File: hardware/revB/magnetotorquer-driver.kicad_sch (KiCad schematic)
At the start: 50 parts, among them J4 T1M-6-F-SV-L, U10 MAX7311AAG+, U11 MCP47FVB24-E/MQ, U12 ALM2402QPWPRQ1, U13 OPA340MDBVTEP, U14 AD7091R-5BCPZ-RL7, U15 ALM2402QPWPRQ1

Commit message: working revB
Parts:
- removed R69, R70, R71: 33, symbol Device:R_US
- added R59 (x2): 1k, Resistor_SMD:R_0603_1608Metric, symbol Device:R_US
- R25, R35, R42: value 10k -> 10Meg
- R65: value 33 -> 1k
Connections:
- net X_Vs_5V: now also U12.2 (IN1+)
- net Y_Vs_5V: now also U12.4 (IN2+)
- net Z_Vs_5V: now also U15.2 (IN1+)
- net ~{AMP_SHDN_XY}: now also R59.1; no longer U12.3 (OTF/SH_DM)
- net ~{AMP_SHDN_Z}: now also R59.1; no longer U15.3 (OTF/SH_DM)
- new net: R59.2, U15.3 (OTF/SH_DM)
- new net: R59.2, U12.3 (OTF/SH_DM)
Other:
- moved on the sheet: C29, R25

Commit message: working revB
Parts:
- removed R30, R31, R41, R43, R59 (x2): 1k, Resistor_SMD:R_0603_1608Metric, symbol Device:R_US
- removed TP1, TP14, TP4, TP7, TP8: TestPoint, TestPoint:TestPoint_Pad_D1.0mm, symbol Connector:TestPoint
- added C49, C51: 10uF, Capacitor_SMD:C_0805_2012Metric, symbol Device:C
- added RN1 (x4): 1k, payload-interface-board:RAVF164D, symbol FP-Interface-Card:R_Network04_US
- renumbered C30 to C16, C29 to C17, C31 to C18, C32 to C19, C33 to C20, C34 to C21, C35 to C22, C36 to C23, C37 to C24, C39 to C25, C40 to C26, C42 to C27, C38 to C28, C41 to C29, C43 to C30, C45 to C31, C46 to C32, R25 to R36, R32 to R39, R33 to R40, R34 to R41, R35 to R42, R36 to R43, R37 to R45, R104 to R46, R38 to R47, R93 to R49, R42 to R50, R39 to R51, R40 to R52, R65 to R55, U12 to U10, U14 to U11, U13 to U12, U15 to U13, U10 to U8, U11 to U9
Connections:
- net +5V: now also C49.1, C51.1
- net ADC_ALERT/BUSY: now also U11.8 (ALERT/BUSY/GPO0), RN1.2; no longer U8.18 (IO_13)
- net DRV_EN_X: now also RN1.2; no longer U8.9 (IO_5)
- net DRV_EN_Y: now also RN1.1; no longer U8.13 (IO_8)
- net DRV_EN_Z: now also RN1.4; no longer U8.16 (IO_11)
- net DRV_PH_X: now also RN1.1; no longer U8.8 (IO_4)
- net DRV_PH_Y: now also RN1.4; no longer U8.11 (IO_7)
- net DRV_PH_Z: now also RN1.3; no longer U8.15 (IO_10)
- net GND: now also C49.2, C51.2
- net ~{ADC_RST}: now also U11.20 (~{RST}), RN1.3; no longer U8.19 (IO_14)
- net ~{AMP_SHDN_XY}: now also U10.3 (OTF/SH_DM), RN1.3; no longer U8.6 (IO_2)
- net ~{AMP_SHDN_Z}: now also U13.3 (OTF/SH_DM), RN1.4; no longer U8.7 (IO_3)
- net ~{DAC_LAT0}: now also U9.18 (~{LAT0}), RN1.1; no longer U8.4 (IO_0)
- net ~{DAC_LAT1}: now also U9.19 (~{LAT1}), RN1.2; no longer U8.5 (IO_1)
- net ~{DRV_SLP_X}: now also RN1.3; no longer U8.10 (IO_6)
- net ~{DRV_SLP_Y}: now also RN1.2; no longer U8.14 (IO_9)
- net ~{DRV_SLP_Z}: now also RN1.1; no longer U8.17 (IO_12)
- net ~{IMU_EN}: now also RN1.4; no longer U8.20 (IO_15)
- new net: RN1.5, U8.7 (IO_3)
- new net: RN1.6, U8.6 (IO_2)
- new net: RN1.7, U8.5 (IO_1)
- new net: RN1.8, U8.4 (IO_0)
- new net: RN1.5, U8.16 (IO_11)
- new net: RN1.6, U8.15 (IO_10)
- new net: RN1.7, U8.14 (IO_9)
- new net: RN1.8, U8.13 (IO_8)
- new net: RN1.5, U8.11 (IO_7)
- new net: RN1.6, U8.10 (IO_6)
- new net: RN1.7, U8.9 (IO_5)
- new net: RN1.8, U8.8 (IO_4)
- new net: RN1.5, U8.20 (IO_15)
- new net: RN1.6, U8.19 (IO_14)
- new net: RN1.7, U8.18 (IO_13)
- new net: RN1.8, U8.17 (IO_12)
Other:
- note removed: "looks weird but is just a unity gain buffer"
- moved on the sheet: C19, C20, C28, C29, R50, R51, R52, U13

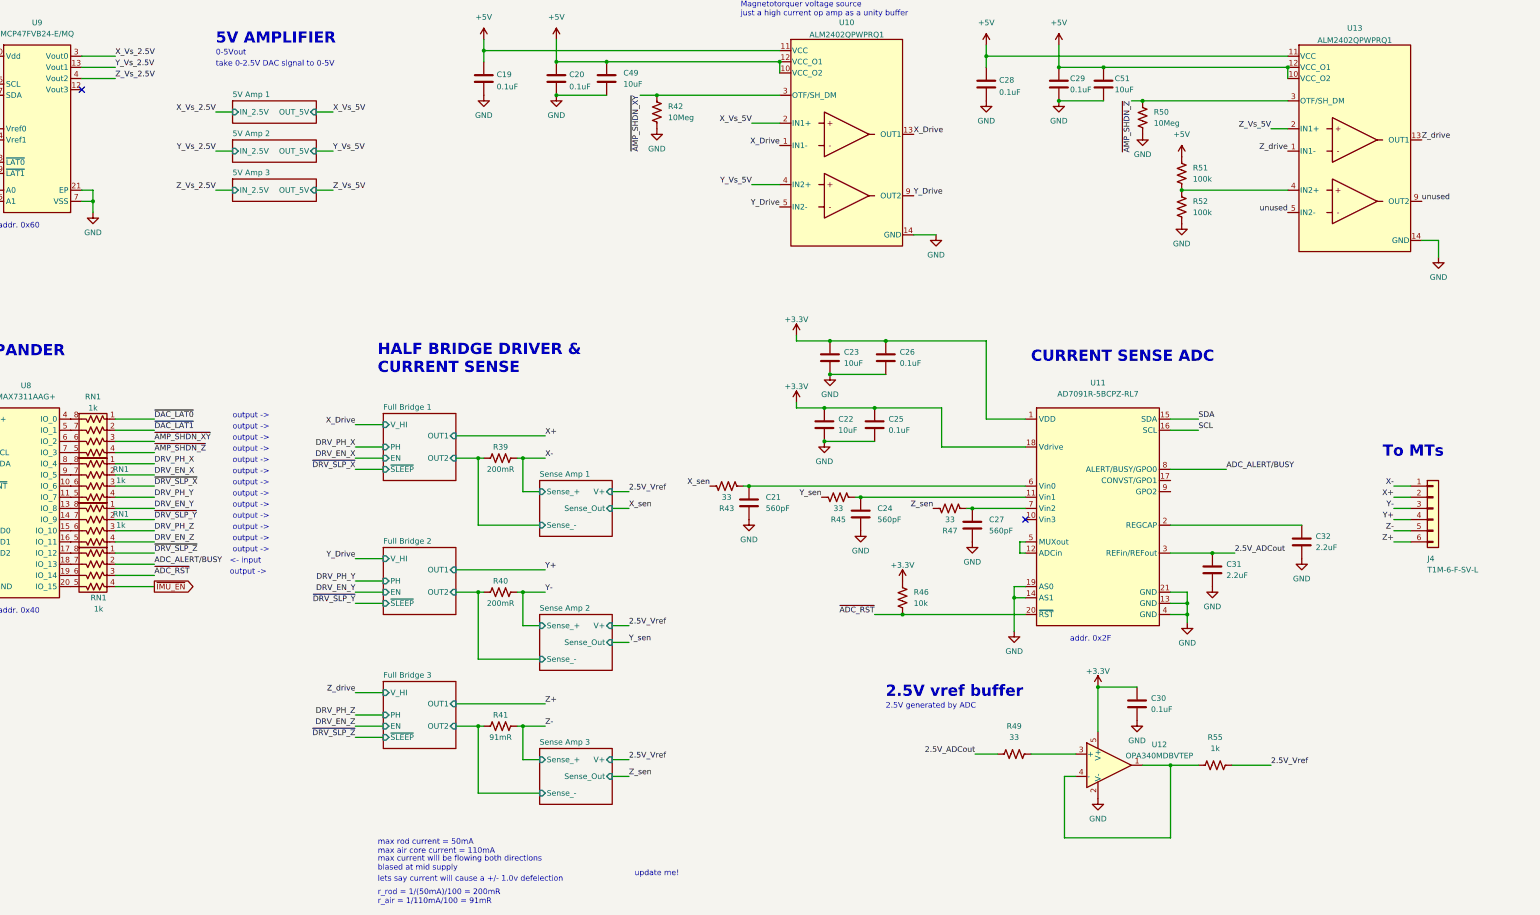
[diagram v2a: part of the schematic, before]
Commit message: updated bp pinout, added payload current sensor
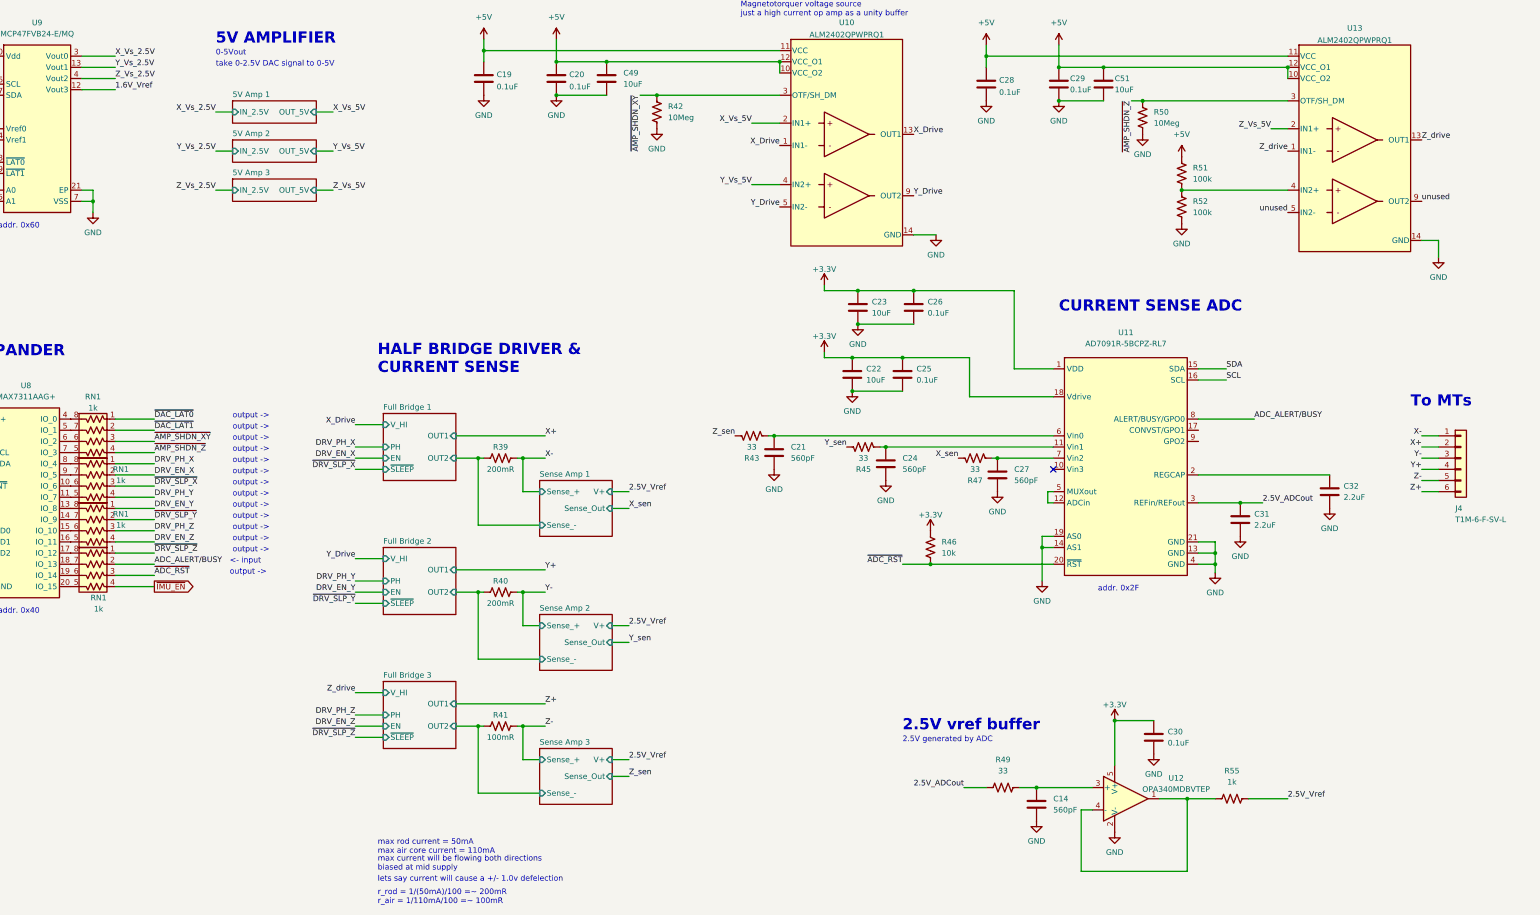
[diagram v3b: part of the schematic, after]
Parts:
- added C14: 560pF, Capacitor_SMD:C_0603_1608Metric, symbol Device:C
- R39, R40: footprint Resistor_SMD:R_0805_2012Metric -> Resistor_SMD:R_2010_5025Metric
- R41: value 91mR -> 100mR; footprint Resistor_SMD:R_0805_2012Metric -> Resistor_SMD:R_2010_5025Metric
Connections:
- net GND: now also C14.1
- net X_sen: now also R47.2; no longer R43.2
- net Z_sen: now also R43.2; no longer R47.2
- net at R49.2, U12.3 (+): now also C14.2
- net 1.6V_Vref: now reaches U9.12 (Vout3)
- no-connect marks 2 -> 1
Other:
- note added: "r_rod = 1/(50mA)/100 =~ 200mR r_air = 1/110mA/100 =~ 100mR"
- note removed: "r_rod = 1/(50mA)/100 = 200mR r_air = 1/110mA/100 = 91mR"
- note removed: "update me!"
- moved on the sheet: C21, C22, C23, C24, C25, C26, C27, C30, C31, C32, J4, R43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

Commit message: updated files
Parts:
- renumbered C16 to C11, C18 to C12, C19 to C13, C20 to C14, C49 to C15, C28 to C16, C29 to C17, C51 to C18, C23 to C19, C26 to C20, C22 to C21, C25 to C22, C17 to C23, C21 to C24, C24 to C25, C27 to C26, C32 to C27, C31 to C28, C30 to C29, C14 to C30, R42 to R21, R50 to R22, R51 to R23, R52 to R24, R43 to R25, R45 to R26, R39 to R27, R47 to R28, R36 to R29, R46 to R30, R40 to R31, R41 to R32, R49 to R33, R55 to R34, U8 to U10, U12 to U11, U9 to U6, U10 to U7, U13 to U8, U11 to U9
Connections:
- net +3V3 renamed +3.3V

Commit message: working
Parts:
- removed C11, C18, C19, C21: 10uF, Capacitor_SMD:C_0805_2012Metric, symbol Device:C
- removed C12, C13, C20, C22, C23, C29: 0.1uF, Capacitor_SMD:C_0603_1608Metric, symbol Device:C
- removed C24, C25, C26, C30: 560pF, Capacitor_SMD:C_0603_1608Metric, symbol Device:C
- removed C27, C28: 2.2uF, Capacitor_SMD:C_0805_2012Metric, symbol Device:C
- removed J4: T1M-6-F-SV-L, payload-interface-board:SAMTEC_T1M-06-F-SV-L, symbol Connector_Generic:Conn_01x06
- removed R21, R22, R29: 10Meg, Resistor_SMD:R_0603_1608Metric, symbol Device:R_US
- removed R23, R24: 100k, Resistor_SMD:R_0603_1608Metric, symbol Device:R_US
- removed R25, R26, R28: 33, Resistor_SMD:R_0603_1608Metric, symbol Device:R_US
- removed R27: 200mR, Resistor_SMD:R_2010_5025Metric, symbol Device:R_US
- removed RN1 (x4): 1k, payload-interface-board:RAVF164D, symbol FP-Interface-Card:R_Network04_US
- removed U10: MAX7311AAG+, Package_SO:SSOP-24_5.3x8.2mm_P0.65mm, symbol FP-Interface-Card:MAX7311AAG+
- removed U11: OPA340MDBVTEP, Package_TO_SOT_SMD:SOT-23-5, symbol Amplifier_Operational:OPA340NA
- removed U6: MCP47FVB24-E/MQ, payload-interface-board:MCP47FVB24EMQ, symbol FP-Interface-Card:MCP47FVB24-E/MQ
- removed U7, U8: ALM2402QPWPRQ1, Package_SO:HTSSOP-14-1EP_4.4x5mm_P0.65mm_EP3.4x5mm_Mask3x3.1mm, symbol magnetotorquer-test-board:ALM2402QPWPRQ1
- removed U9: AD7091R-5BCPZ-RL7, Package_DFN_QFN:QFN-20-1EP_4x4mm_P0.5mm_EP2.5x2.5mm, symbol FP-Interface-Card:AD7091R-5BCPZ-RL7
- added C4: 10uF, Capacitor_SMD:C_0805_2012Metric, symbol Device:C
- added D7: SP1326-01LTG, Diode_SMD:D_SOD-523, symbol Device:D_TVS
- added R35, R37: 1k, Resistor_SMD:R_0402_1005Metric, symbol Device:R_US
- added R36: 100k, Resistor_SMD:R_0402_1005Metric, symbol Device:R_US
- added U7: TLV4110xDGN, Package_SO:MSOP-8-1EP_3x3mm_P0.65mm_EP1.68x1.88mm, symbol SierraLobo:TLV4110xDGN
- added U8: DRV8838DSGT, Package_SON:WSON-8-1EP_2x2mm_P0.5mm_EP0.9x1.6mm, symbol magnetotorquer-test-board:DRV8838DSGT
- added U9: INA199A2xDCK, Package_TO_SOT_SMD:SOT-363_SC-70-6, symbol Amplifier_Current:INA199xxDCK
- C14, C17: footprint Capacitor_SMD:C_0603_1608Metric -> Capacitor_SMD:C_0402_1005Metric; Manufacturer (none) -> TDK; Mfr. Part No (none) -> CGA2B3X7R1H104K050BE
- C15: value 10uF -> 0.1uF; footprint Capacitor_SMD:C_0805_2012Metric -> Capacitor_SMD:C_0402_1005Metric; Manufacturer (none) -> TDK; Mfr. Part No (none) -> CGA2B3X7R1H104K050BE
- C16: value 0.1uF -> 0.01uF; footprint Capacitor_SMD:C_0603_1608Metric -> Capacitor_SMD:C_0402_1005Metric
- R30: value 10k -> 110k
- R31: value 200mR -> 1k; footprint Resistor_SMD:R_2010_5025Metric -> Resistor_SMD:R_0402_1005Metric
- R32: value 100mR -> 100k; footprint Resistor_SMD:R_2010_5025Metric -> Resistor_SMD:R_0402_1005Metric
- R33: value 33 -> 110k
- R34: footprint Resistor_SMD:R_0603_1608Metric -> Resistor_SMD:R_0402_1005Metric
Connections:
- net Full Bridge 3/OUT2 is gone; now on net GND: R32.1
- net Z- is gone; now on net ~{AMP_SHDN}: R32.2
- net GND: now also C4.2, R36.1, U7.4 (V-), U8.4 (GND), U8.9 (GND), U9.2 (GND)
- net DRIVE: now reaches R33.2
- net DRIVE: now also U7.6, U8.1 (VM)
- net ~{HB_SLEEP}: now reaches R34.1
- net ~{HB_SLEEP}: now also R36.2
- net +3.3V: no longer names the net of R30.2
- net +3.3V: now also U7.3 (+)
- net +5V renamed 3V3_ADC
- net 3V3_ADC: now also U9.3 (V+); no longer C14.1, C15.1
- net 2.5V_ADCout: no longer names the net of R33.1
- net 2.5V_ADCout: now also U7.2 (-)
- net 2.5V_Vref: no longer names the net of R34.2
- net 2.5V_Vref: now also U8.7 (~{SLEEP})
- net Full Bridge 2/OUT2: no longer names the net of R31.1
- net Full Bridge 2/OUT2: now also U7.8 (~{SHDN})
- net Y- renamed ~{AMP_SHDN}
- net ~{ADC_RST} renamed DRV_IN
- new net: R35.2, U8.6 (PH)
- new net: R37.2, U8.5 (EN)
- new net 1V65A: U9.1 (REF)
- new net 3V3D: C15.1, U8.8 (VCC)
- new net 5VA: C14.1, C4.1, U7.7 (V+)
- new net HB_EN: R37.1
- new net HB_PH: R35.1
- new net ISENSE: U9.6
- new net OUT1: D7.2 (A2), U8.2 (OUT1), U9.4 (+)
- new net OUT2: D7.1 (A1), U8.3 (OUT2)
- new net SENSE: U9.5 (-)
- no-connect marks 1 -> 0
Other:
- removed sheet 5V Amp 1
- removed sheet 5V Amp 2
- removed sheet 5V Amp 3
- removed sheet Full Bridge 1
- removed sheet Full Bridge 2
- removed sheet Full Bridge 3
- removed sheet Sense Amp 1
- removed sheet Sense Amp 2
- removed sheet Sense Amp 3
- note added: "100v/v gain"
- note added: "Amplify DAC power output"
- note added: "CURRENT SENSE AMP"
- note added: "DAC_IN = 0-5V X/Y MTQ resistance = 80-145R, 0.2W rated Z MTQ resistance = 30-55R, 0.57W Maximum output current control should be limited by MTQ power (0.2W) -> Ioutmax(X,Y) = 50mA (80R, 0.2W) -> Ioutmax(Z) = 137mA (30R, 0.57W)"
- note added: "FET Back diodes in full bridge should clamp drive voltage"
- note added: "HALF BRIDGE DRIVER"
- note added: "PARAMATERS"
- note added: "POWER AMP"
- note added: "Select Rsense to give 1.5V deflection at Imax"
- note added: "Sense resistor at higher level sheet"
- note added: "VMID is mid-supply of VADC (1.65V)"
- note added: "current sense amplifier"
- note added: "for bi-directional control"
- note added: "read current output"
- note removed: "0-2.5Vout"
- note removed: "0-5Vout"
- note removed: "2.5V generated by ADC"
- note removed: "2.5V vref buffer"
- note removed: "5V AMPLIFIER"
- note removed: "<- input"
- note removed: "CURRENT SENSE ADC"
- note removed: "DAC STAGE"
- note removed: "DRIVE AMPLIFIER"
- note removed: "HALF BRIDGE DRIVER & CURRENT SENSE"
- note removed: "IO EXPANDER"
- note removed: "Magnetotorquer voltage source just a high current op amp as a unity buffer"
- note removed: "To MTs"
- note removed: "addr. 0x2F"
- note removed: "addr. 0x40"
- note removed: "addr. 0x60"
- note removed: "lets say current will cause a +/- 1.0v defelection"
- note removed: "max current will be flowing both directions biased at mid supply"
- note removed: "max rod current = 50mA max air core current = 110mA"
- note removed: "output ->"
- note removed: "r_rod = 1/(50mA)/100 =~ 200mR r_air = 1/110mA/100 =~ 100mR"
- note removed: "take 0-2.5V DAC signal to 0-5V"
- company: Sierra Lobo INC -> (none)
- title: (none) -> Foras Promineo Payload Interface Board
